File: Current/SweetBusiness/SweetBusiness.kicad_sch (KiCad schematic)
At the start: 42 parts, among them J0 USB, J2 I2C, U0 STM32F411RETx, U1 LDO-3.3, Y1 8MHz

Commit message: Hard Light Micro 5, Borealis, 2T, SB
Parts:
- added U2: USBLC6-2SC6, Package_TO_SOT_SMD:SOT-23-6, symbol Power_Protection:USBLC6-2SC6
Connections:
- net D+: now also U2.6 (I/O1); no longer U0.45 (PA12)
- net D-: now also U2.4 (I/O2); no longer U0.44 (PA11)
- net GND: now also U0.12 (VSSA), U0.18 (VSS), U2.2 (GND)
- net VBUS: now also U2.5 (VBUS)
- net enc1A: no longer names the net of U0.54 (PD2)
- net enc1B: no longer names the net of U0.55 (PB3)
- new net DB+: U0.45 (PA12), U2.1 (I/O1)
- new net DB-: U0.44 (PA11), U2.3 (I/O2)
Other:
- note added: "ESD Isolator"
- moved on the sheet: C1, C2, C3, C4, C5, C6, C9, CL1, CL2, CV1, F0, H1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

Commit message: Nice changelog, idiot.
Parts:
- removed U2: USBLC6-2SC6, Package_TO_SOT_SMD:SOT-23-6, symbol Power_Protection:USBLC6-2SC6
- added J3: Bridge, Connector_PinHeader_2.54mm:PinHeader_2x04_P2.54mm_Vertical, symbol Connector_Generic:Conn_02x04_Odd_Even
- H1, H2, H3, H4, H5, H6, H7, H8: footprint MountingHole:MountingHole_2.7mm_M2.5_ISO14580_Pad -> EDI:SolderableHole-M2
- KL1, KL2, KL3: footprint LED_SMD:LED_0603_1608Metric_Pad1.05x0.95mm_HandSolder -> LED_THT:LED_D1.8mm_W3.3mm_H2.4mm
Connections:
- net DB+ is gone; now on net D+: U0.45 (PA12)
- net DB- is gone; now on net D-: U0.44 (PA11)
- net +3V3: no longer KL1.2 (A), KL2.2 (A), KL3.2 (A)
- net GND: now also KL1.1 (K), KL2.1 (K), KL3.1 (K), J3.4 (Pin_4), J3.6 (Pin_6), J3.8 (Pin_8)
- net VBUS: now also J3.1 (Pin_1), J3.3 (Pin_3), J3.5 (Pin_5), J3.7 (Pin_7)
- net col0: now also U0.41 (PA8)
- net col1: now also U0.40 (PC9)
- net col10: now also U0.26 (PB0)
- net col11: now also U0.25 (PC5)
- net col12: now also U0.24 (PC4)
- net col13: now also U0.23 (PA7)
- net col14: now also U0.22 (PA6)
- net col15: now also U0.21 (PA5)
- net col16: now also U0.20 (PA4)
- net col17: now also U0.17 (PA3)
- net col18: now also U0.16 (PA2)
- net col19: now also U0.15 (PA1)
- net col2: now also U0.39 (PC8)
- net col20: now also U0.11 (PC3)
- net col21: now also U0.10 (PC2)
- net col22: now also U0.9 (PC1)
- net col3: now also U0.38 (PC7)
- net col4: now also U0.37 (PC6)
- net col5: now also U0.36 (PB15)
- net col6: now also U0.35 (PB14)
- net col7: now also U0.34 (PB13)
- net col8: now also U0.33 (PB12)
- net col9: now also U0.27 (PB1)
- net row0: now also U0.56 (PB4)
- net row1: now also U0.57 (PB5)
- net row2: now also U0.61 (PB8)
- net row3: now also U0.62 (PB9)
- net row4: now also U0.2 (PC13)
- net row5: now also U0.3 (PC14)
- net row6: now also U0.4 (PC15)
- net at RL1.1: now also KL1.2 (A); no longer KL1.1 (K)
- net at RL2.1: now also KL2.2 (A); no longer KL2.1 (K)
- net at RL3.1: now also KL3.2 (A); no longer KL3.1 (K)
- net LED: now reaches U0.14 (PA0)
- net LED: now also J3.2 (Pin_2)
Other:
- note removed: "ESD Isolator"
- moved on the sheet: KL1, KL2, KL3

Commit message: oh my god just stop
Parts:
- removed C7: 10uF, EDI:Passive_0402_1005Metric, symbol Device:C_Small
- removed U1: LDO-3.3, Package_TO_SOT_SMD:SOT-23, symbol Regulator_Linear:LD1117S33TR_SOT223
- added CP1: 100nF, EDI:Passive_0402_1005Metric, symbol Device:C_Small
- added CP10, CP11, CP12, CP13, CP14, CP15, CP16, CP17, CP2, CP3, CP4, CP5, CP6, CP7, CP8: 22uf, EDI:Passive_0402_1005Metric, symbol Device:C_Small
- added LP1: 10uH, Inductor_SMD:L_Wuerth_HCI-1040, symbol Device:L
- added RP1: 100K, EDI:Passive_0402_1005Metric, symbol Device:R_Small
- added RP2: 22.1K, EDI:Passive_0402_1005Metric, symbol Device:R_Small
- added U1: MT2492, Package_TO_SOT_SMD:SOT-23-6, symbol EDI:MT2492
- CP9: renamed from C8; value 100nF -> 22uf; LCSC C1525 -> C415703
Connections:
- net +3V3: now also J3.1 (Pin_1), J3.3 (Pin_3), J3.5 (Pin_5), J3.7 (Pin_7), CP10.1, CP11.1, CP12.1, CP13.1, CP14.1, CP15.1, CP16.1, CP17.1, LP1.2, RP1.1
- net GND: now also CP10.2, CP11.2, CP12.2, CP13.2, CP14.2, CP15.2, CP16.2, CP17.2, CP2.1, CP3.1, CP4.1, CP5.1, CP6.1, CP7.1, CP8.1, RP2.2, U1.2 (GND)
- net VBUS: now also CP2.2, CP3.2, CP4.2, CP5.2, CP6.2, CP7.2, CP8.2, U1.4 (EN), U1.5 (VIN); no longer J3.1 (Pin_1), J3.3 (Pin_3), J3.5 (Pin_5), J3.7 (Pin_7)
- new net: RP1.2, RP2.1, U1.3 (FB)
- new net: CP1.1, U1.1 (BS)
- new net: CP1.2, LP1.1, U1.6 (SW)
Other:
- moved on the sheet: CP9, J3

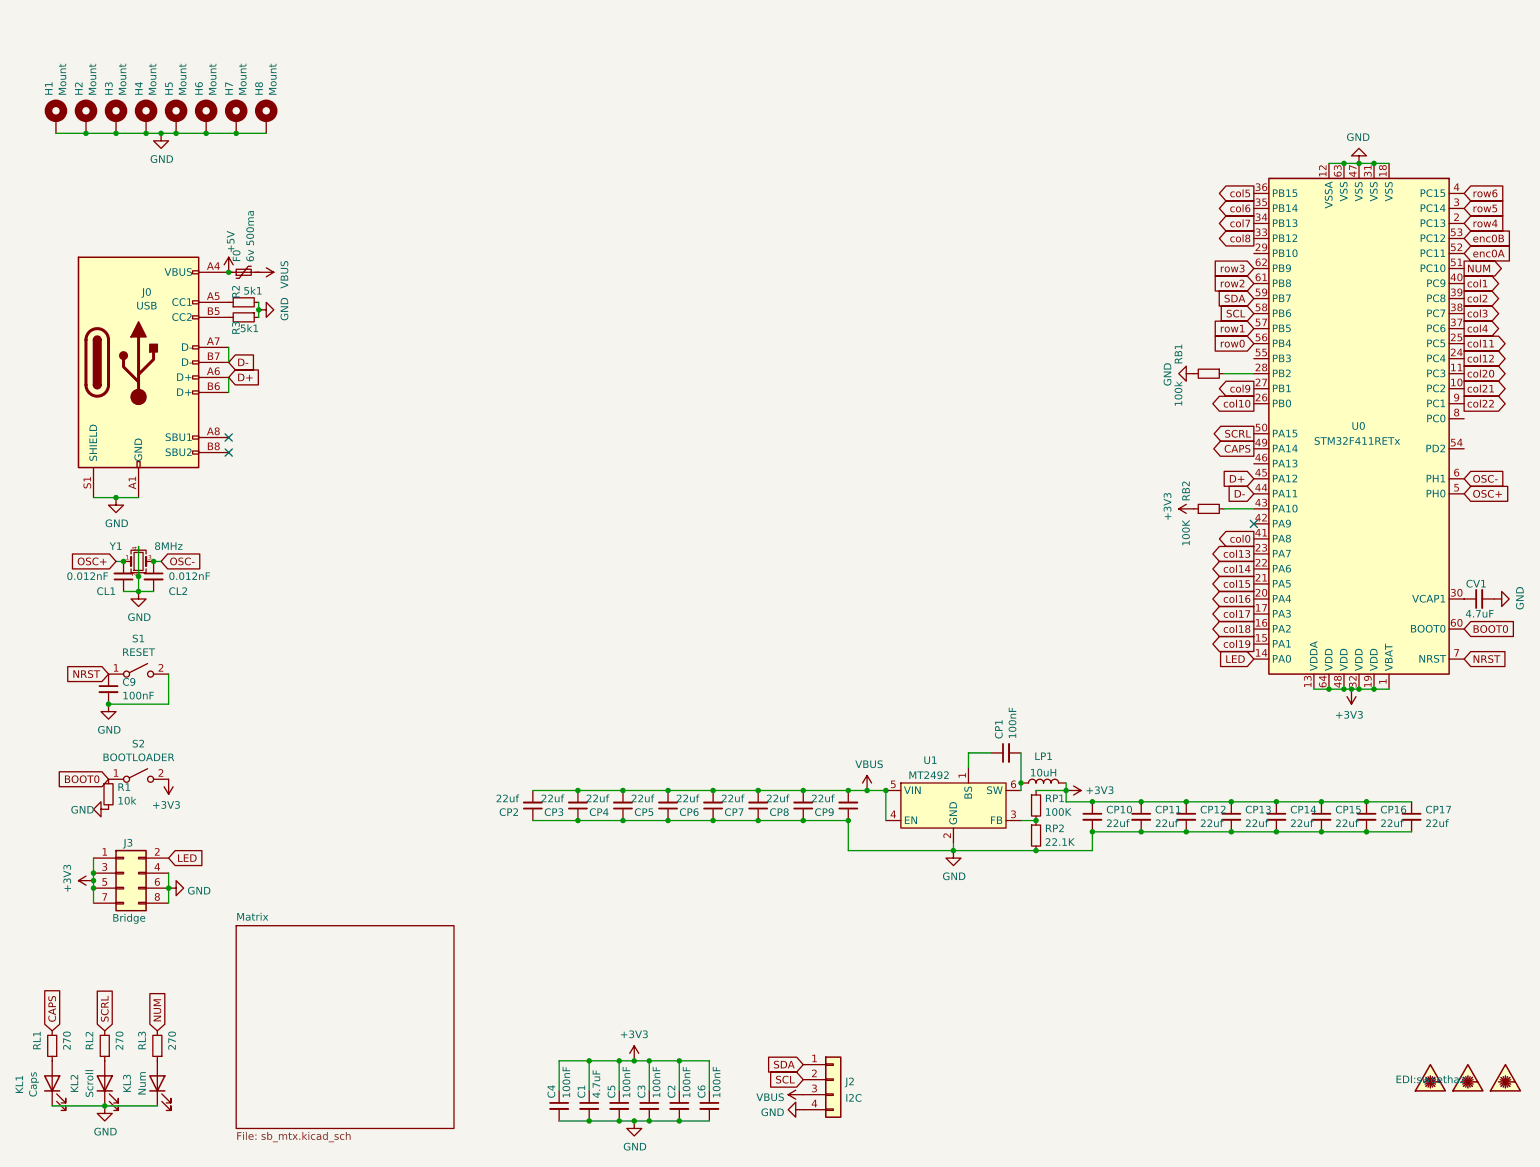
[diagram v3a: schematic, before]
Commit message: Yep, moved some stuff to archives.
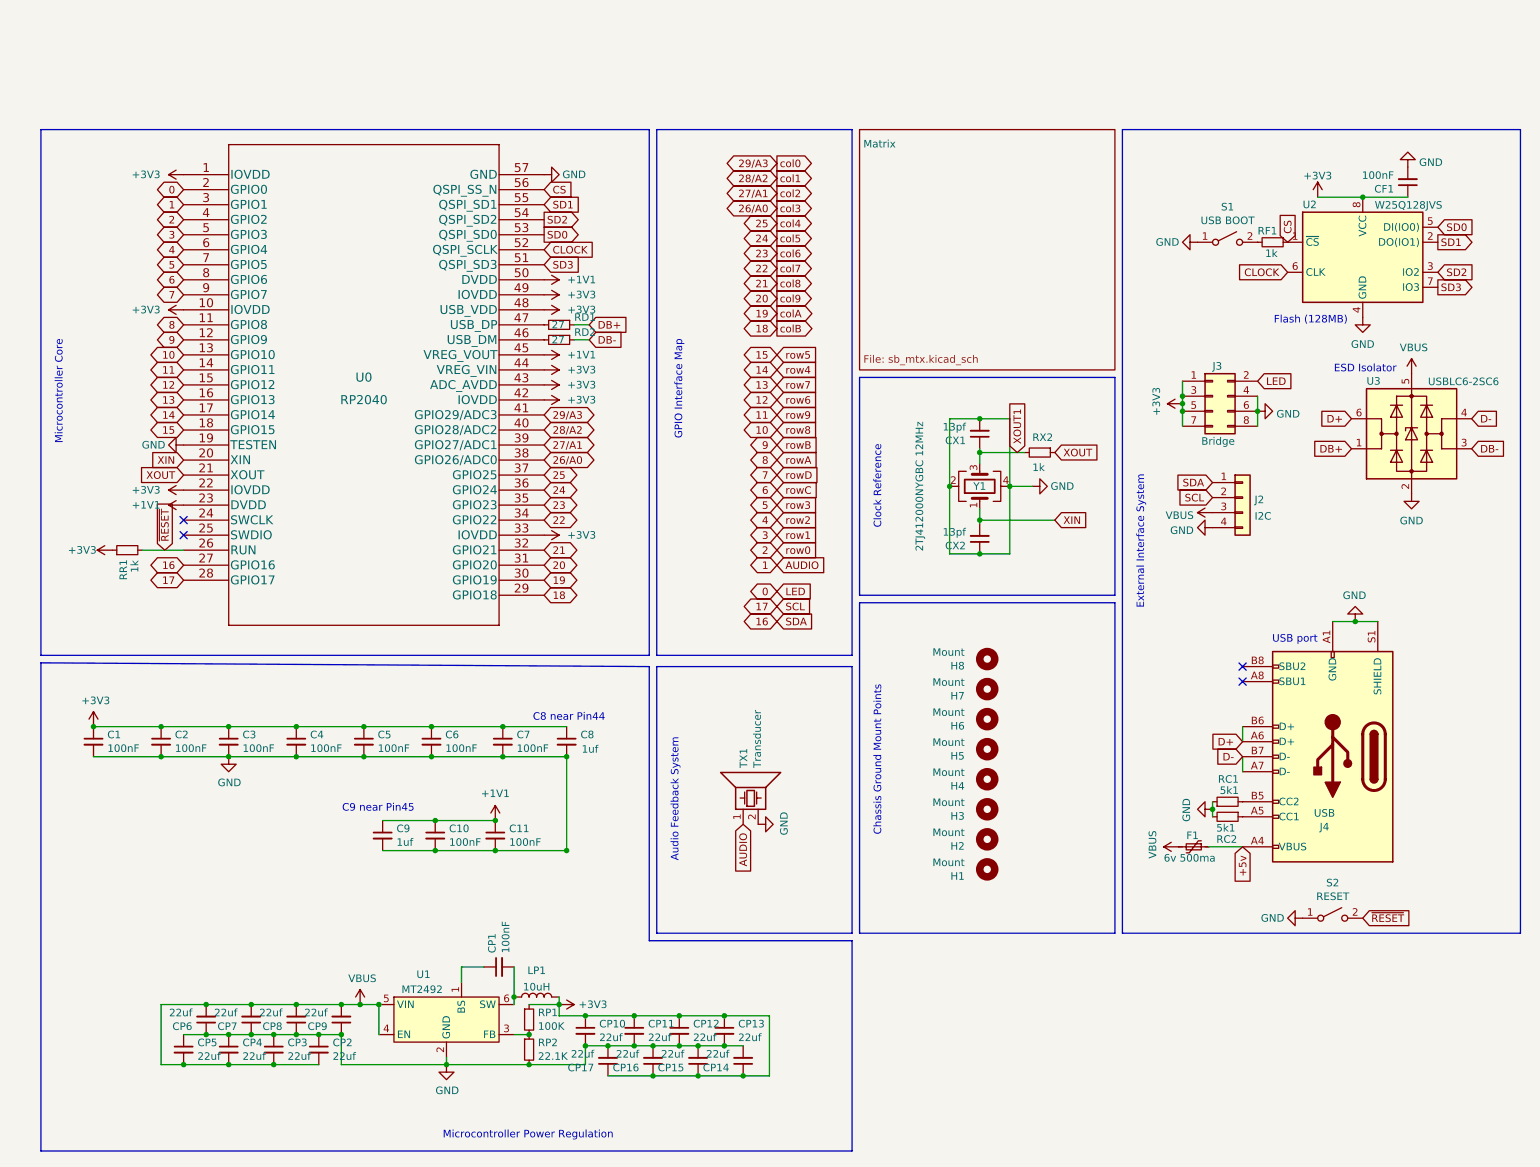
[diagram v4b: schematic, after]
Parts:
- removed CL1, CL2: 0.012nF, EDI:Passive_0402_1005Metric, symbol Device:C_Small
- removed CV1: 4.7uF, EDI:Passive_0402_1005Metric, symbol Device:C_Small
- removed F0: 6v 500ma, Fuse:Fuse_0603_1608Metric, symbol Device:Polyfuse_Small
- removed J0: USB, Connector_USB:USB_C_Receptacle_HRO_TYPE-C-31-M-12, symbol HL-Mk3-rescue:USB_C_Receptacle_USB2.0-Connector-HL-Mk2-rescue
- removed KL1: Caps, LED_THT:LED_D1.8mm_W3.3mm_H2.4mm, symbol Device:LED
- removed KL2: Scroll, LED_THT:LED_D1.8mm_W3.3mm_H2.4mm, symbol Device:LED
- removed KL3: Num, LED_THT:LED_D1.8mm_W3.3mm_H2.4mm, symbol Device:LED
- removed R1: 10k, EDI:Passive_0402_1005Metric, symbol Device:R_Small
- removed R2, R3: 5k1, EDI:Passive_0402_1005Metric, symbol Device:R_Small
- removed RB1: 100k, EDI:Passive_0402_1005Metric, symbol Device:R_Small
- removed RB2: 100K, EDI:Passive_0402_1005Metric, symbol Device:R_Small
- removed RL1, RL2, RL3: 270, EDI:Passive_0402_1005Metric, symbol Device:R_Small
- removed U0: STM32F411RETx, Package_QFP:LQFP-64_10x10mm_P0.5mm, symbol MCU_ST_STM32F4:STM32F411RETx
- removed Y1: 8MHz, Crystal:Crystal_SMD_3225-4Pin_3.2x2.5mm, symbol Device:Crystal_GND24_Small
- removed Z0: SweetBiz ID, EDI:EDI-HP-SCI, symbol Graphic:SYM_LASER_Small
- removed Z1: Business Time, EDI:mk5-sweetbiz, symbol Graphic:SYM_LASER_Small
- removed Z2: SweetBiz ID, EDI:sweethaz, symbol Graphic:SYM_LASER_Small
- added C10, C11, C7, CF1: 100nF, EDI:Passive_0402_1005Metric, symbol Device:C_Small
- added C8: 1uf, EDI:Passive_0402_1005Metric, symbol Device:C_Small
- added CX1, CX2: 13pf, EDI:Passive_0402_1005Metric, symbol Device:C_Small
- added F1: 6v 500ma, Fuse:Fuse_0603_1608Metric, symbol Device:Polyfuse_Small
- added J4: USB, Connector_USB:USB_C_Receptacle_HRO_TYPE-C-31-M-12, symbol HL-Mk2-rescue:USB_C_Receptacle_USB2.0-Connector
- added RC1, RC2: 5k1, EDI:Passive_0402_1005Metric, symbol Device:R_Small
- added RD1, RD2: 27, EDI:Passive_0402_1005Metric, symbol Device:R_Small
- added RF1, RR1, RX2: 1k, EDI:Passive_0402_1005Metric, symbol Device:R_Small
- added TX1: Transducer, Buzzer_Beeper:Buzzer_CUI_CPT-9019S-SMT, symbol Device:Speaker_Crystal
- added U0: RP2040, EDI:QFN-56-RP2040, symbol RP2040:RP2040
- added U2: W25Q128JVS, Package_SO:SOIC-8_5.23x5.23mm_P1.27mm, symbol Memory_Flash:W25Q128JVS
- added U3: USBLC6-2SC6, Package_TO_SOT_SMD:SOT-23-6, symbol Power_Protection:USBLC6-2SC6
- added Y1: 2TJ412000NYGBC 12MHz, Crystal:Crystal_SMD_2520-4Pin_2.5x2.0mm, symbol Device:Crystal_GND24
- C1: value 4.7uF -> 100nF; LCSC C23733 -> C1525
- C9: value 100nF -> 1uf; LCSC C1525 -> C52923
- H1, H2, H3, H4, H5, H6, H7, H8: footprint EDI:SolderableHole-M2 -> MountingHole:MountingHole_3.2mm_M3; symbol Mechanical:MountingHole_Pad -> Mechanical:MountingHole
- S1: value RESET -> USB BOOT; LCSC C115351 -> C139779
- S2: value BOOTLOADER -> RESET; LCSC C115351 -> C139779
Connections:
- net BOOT0 is gone; now on net GND: S2.1 (A)
- net +3V3: now also C7.1, C8.1, CF1.1, RR1.1, U0.1 (IOVDD), U0.10 (IOVDD), U0.22 (IOVDD), U0.33 (IOVDD), U0.42 (IOVDD), U0.43 (ADC_AVDD), U0.44 (VREG_VIN), U0.48 (USB_VDD), U0.49 (IOVDD), U2.8 (VCC); no longer S2.2 (B)
- net D+: now also J4.A6 (D+), J4.B6 (D+), U3.6 (I/O1)
- net D-: now also J4.A7 (D-), J4.B7 (D-), U3.4 (I/O2)
- net GND: now also S1.1 (A), C10.2, C11.2, C7.2, C8.2, CF1.2, CX1.2, CX2.1, J4.A1 (GND), J4.A12 (GND), J4.B1 (GND), J4.B12 (GND), J4.S1 (SHIELD), RC1.1, RC2.2, TX1.2, U0.19 (TESTEN), U0.57 (GND), U2.4 (GND), U3.2 (GND), Y1.2, Y1.4; no longer H1.1, H2.1, H3.1, H4.1, H5.1, H6.1, H7.1, H8.1, S1.2 (B)
- net VBUS: now also F1.2, U3.5 (VBUS)
- net LED renamed 0
- net 0: now also U0.2 (GPIO0)
- net NRST renamed +1V1
- net +1V1: now also C10.1, C11.1, U0.23 (DVDD), U0.45 (VREG_VOUT), U0.50 (DVDD); no longer S1.1 (A)
- net SCL renamed 17
- net 17: now also U0.28 (GPIO17)
- net SDA renamed 16
- net 16: now also U0.27 (GPIO16)
- new net: RD1.2, U0.47 (USB_DP)
- new net: J4.B5 (CC2), RC1.2
- new net: RD2.2, U0.46 (USB_DM)
- new net: J4.A5 (CC1), RC2.1
- new net: RF1.2, S1.2 (B)
- new net +5v: F1.1, J4.A4 (VBUS), J4.A9 (VBUS), J4.B4 (VBUS), J4.B9 (VBUS)
- new net 1: TX1.1, U0.3 (GPIO1)
- new net 10: U0.13 (GPIO10)
- new net 11: U0.14 (GPIO11)
- new net 12: U0.15 (GPIO12)
- new net 13: U0.16 (GPIO13)
- new net 14: U0.17 (GPIO14)
- new net 15: U0.18 (GPIO15)
- new net 18: U0.29 (GPIO18)
- new net 19: U0.30 (GPIO19)
- new net 2: U0.4 (GPIO2)
- new net 20: U0.31 (GPIO20)
- new net 21: U0.32 (GPIO21)
- new net 22: U0.34 (GPIO22)
- new net 23: U0.35 (GPIO23)
- new net 24: U0.36 (GPIO24)
- new net 25: U0.37 (GPIO25)
- new net 26/A0: U0.38 (GPIO26/ADC0)
- new net 27/A1: U0.39 (GPIO27/ADC1)
- new net 28/A2: U0.40 (GPIO28/ADC2)
- new net 29/A3: U0.41 (GPIO29/ADC3)
- new net 3: U0.5 (GPIO3)
- new net 4: U0.6 (GPIO4)
- new net 5: U0.7 (GPIO5)
- new net 6: U0.8 (GPIO6)
- new net 7: U0.9 (GPIO7)
- new net 8: U0.11 (GPIO8)
- new net 9: U0.12 (GPIO9)
- new net CLOCK: U0.52 (QSPI_SCLK), U2.6 (CLK)
- new net CS: RF1.1, U0.56 (QSPI_SS_N), U2.1 (~{CS})
- new net DB+: RD1.1, U3.1 (I/O1)
- new net DB-: RD2.1, U3.3 (I/O2)
- new net SD0: U0.53 (QSPI_SD0), U2.5 (DI(IO0))
- new net SD1: U0.55 (QSPI_SD1), U2.2 (DO(IO1))
- new net SD2: U0.54 (QSPI_SD2), U2.3 (IO2)
- new net SD3: U0.51 (QSPI_SD3), U2.7 (IO3)
- new net XIN: CX2.2, U0.20 (XIN), Y1.1
- new net XOUT: RX2.1, U0.21 (XOUT)
- new net XOUT1: CX1.1, RX2.2, Y1.3
- new net ~{RESET}: RR1.2, S2.2 (B), U0.26 (RUN)
- no-connect marks 3 -> 4
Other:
- note added: "Audio Feedback System"
- note added: "C8 near Pin44"
- note added: "C9 near Pin45"
- note added: "Chassis Ground Mount Points"
- note added: "Clock Reference"
- note added: "ESD Isolator"
- note added: "External Interface System"
- note added: "Flash (128MB)"
- note added: "GPIO Interface Map"
- note added: "Microcontroller Core"
- note added: "Microcontroller Power Regulation"
- note added: "USB port"
- moved on the sheet: CP1, CP10, CP11, CP12, CP13, CP14, CP15, CP16, CP17, CP2, CP3, CP4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

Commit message: So much stuff
Wow it's been a while.
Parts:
- removed CX1, CX2: 13pf, EDI:Passive_0402_1005Metric, symbol Device:C_Small
- removed J3: Bridge, Connector_PinHeader_2.54mm:PinHeader_2x04_P2.54mm_Vertical, symbol Connector_Generic:Conn_02x04_Odd_Even
- removed S1: USB BOOT, Button_Switch_SMD:SW_SPST_SKQG_WithoutStem, symbol Switch:SW_SPST
- removed TX1: Transducer, Buzzer_Beeper:Buzzer_CUI_CPT-9019S-SMT, symbol Device:Speaker_Crystal
- removed Y1: 2TJ412000NYGBC 12MHz, Crystal:Crystal_SMD_2520-4Pin_2.5x2.0mm, symbol Device:Crystal_GND24
- added TX0: Transducer, Buzzer_Beeper:Buzzer_CUI_CPT-9019S-SMT, symbol Device:Speaker_Crystal
- added Y0: CSTCE12M0G55-R0, Crystal:Resonator_SMD_Murata_CSTxExxV-3Pin_3.0x1.1mm, symbol Device:Crystal_GND2_Small
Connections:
- net +3V3: now also J2.3 (Pin_3)
- net 1: now also TX0.1
- net GND: now also RF1.2, TX0.2, Y0.2
- net VBUS: no longer J2.3 (Pin_3)
- net XIN: now also Y0.1
- net XOUT1: no longer names the net of RX2.2
- net XOUT1: now also Y0.3
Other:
- note added: "Chassis Accessory Mount Points"
- note added: "I2C Interface Expander"
- note removed: "Audio Feedback System"
- note removed: "Chassis Ground Mount Points"
- moved on the sheet: C1, C10, C11, C2, C3, C4, C5, C6, C7, C8, C9, CF1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

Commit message: Bulk catchup commit 2023-01-21
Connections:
- net 1: no longer TX0.1
- net 16: no longer J2.1 (Pin_1)
- net 17: no longer J2.2 (Pin_2)
- net 26/A0: now also TX0.1
- net 28/A2: now also J2.1 (Pin_1)
- net 29/A3: now also J2.2 (Pin_2)
